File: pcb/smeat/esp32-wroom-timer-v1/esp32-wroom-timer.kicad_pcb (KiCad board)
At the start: 2 copper layers, 49.5 x 51.2 mm, 56 parts, among them J1 Fan_connector, J2 Conn_01x06_Male, J3 input power, Q1 Q_NMOS_GSD, Q2 Q_NMOS_GSD, U1 ESP32-WROOM-32, U2 AMS1117, U3 RX5808, U4 MP1584, U5 RX5808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

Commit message: Update.
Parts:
- added C23: 10µF, Capacitor_SMD:C_0805_2012Metric, B.Cu at (56.8, 60.5)
- added C24: 10µF, Capacitor_SMD:C_0805_2012Metric, B.Cu at (56.8, 63.8)
- R1, R11, R2: value R -> 100k
- R10: value R -> 40.2k
- R12: value R -> 240
- R13: value R -> 390
- R14, R4, R7: value R -> 10k
- R15, R16, R5: value R -> 1k
- R6: value R -> 240k
- R8: value R -> 59k
- R9: value R -> 210k
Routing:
- net GND: track 83.3 -> 89.3 mm, vias 207 -> 208
- net +3V3: track 58.6 -> 61.8 mm

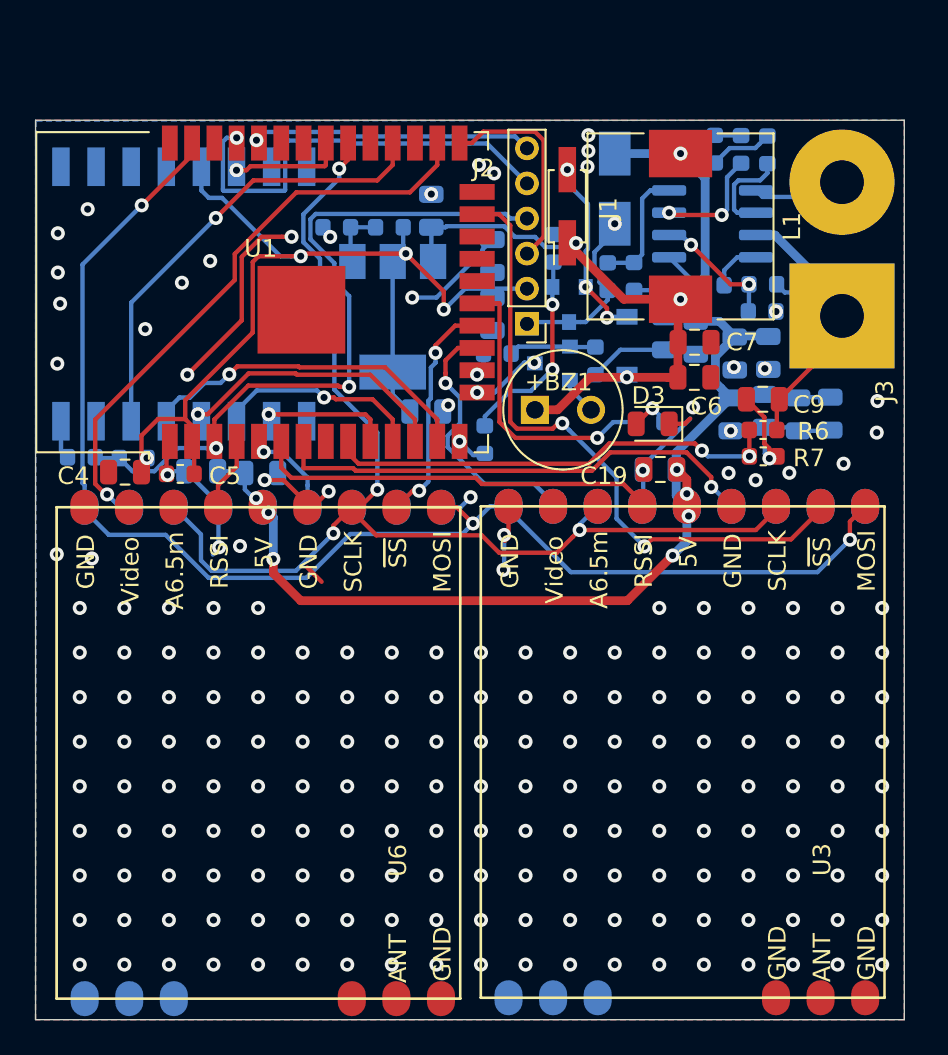
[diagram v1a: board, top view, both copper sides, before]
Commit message: Add a lonely m2 mounting hole Absolutely no space for more than that.
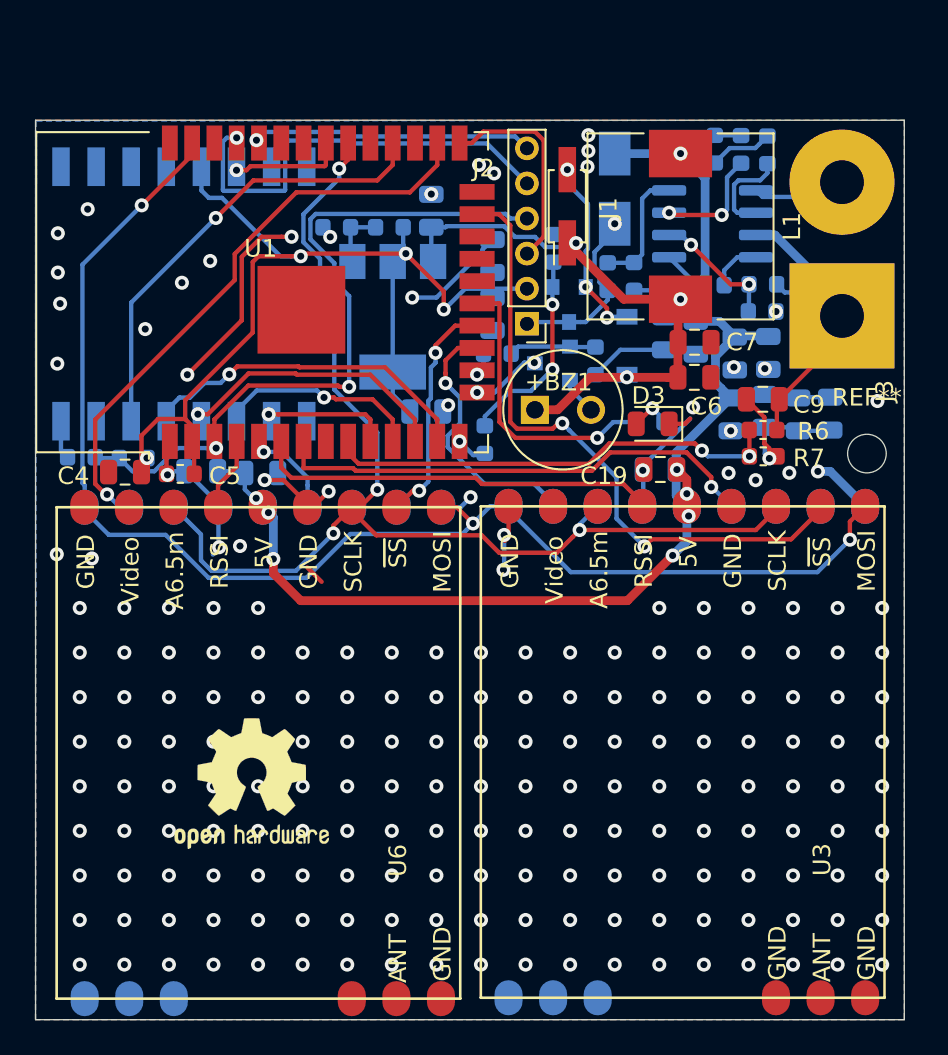
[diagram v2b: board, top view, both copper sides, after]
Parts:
- added REF**: MountingHole_2.2mm_M2, MountingHole:MountingHole_2.2mm_M2, F.Cu at (78.1, 71.8)
- added REF**: OSHW-Logo2_9.8x8mm_SilkScreen, Symbol:OSHW-Logo2_9.8x8mm_SilkScreen, F.Cu at (43.1, 90.6)
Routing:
- net GND: track 89.3 -> 92.8 mm, vias 208 -> 207

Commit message: Disconnect antenna ground from the global ground plane.
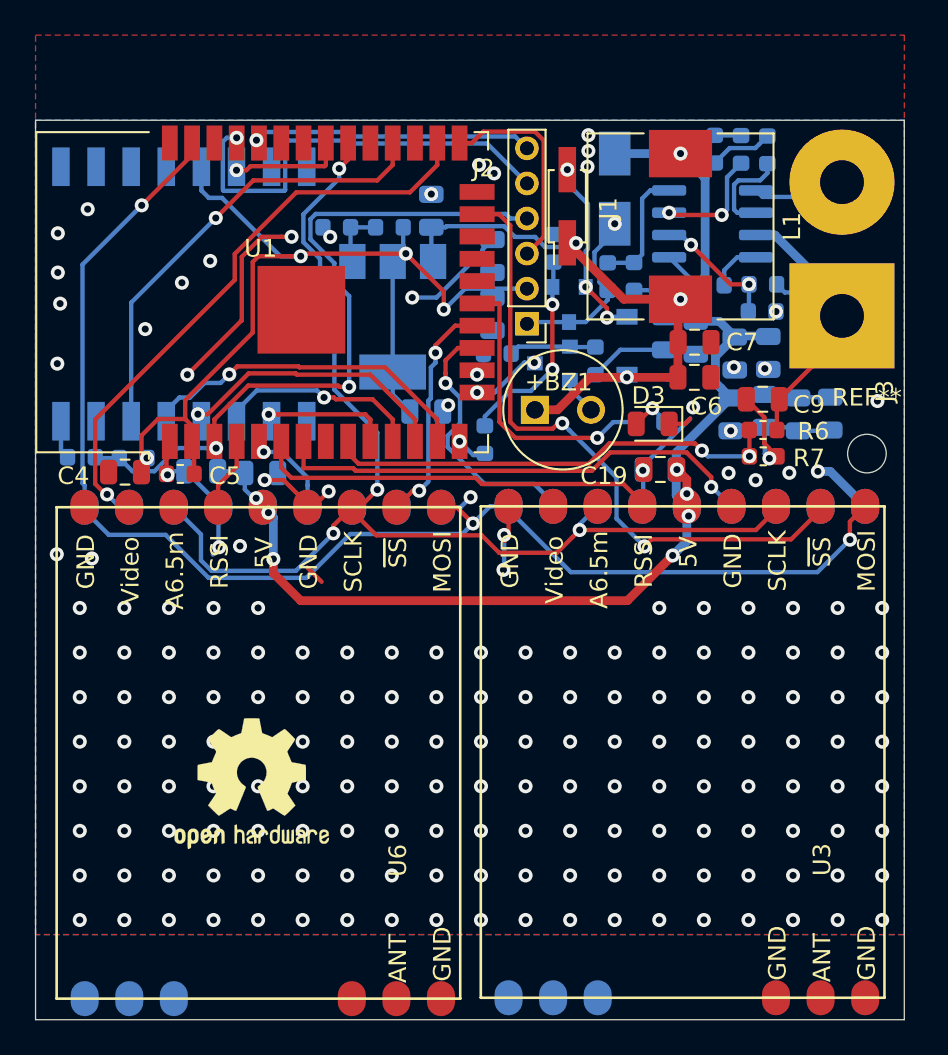
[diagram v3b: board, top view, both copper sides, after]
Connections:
- U3 pad 10: GND -> Net-(U3-Pad10)
- U3 pad 12: GND -> Net-(U3-Pad12)
- U5 pad 10: GND -> Net-(U5-Pad10)
- U5 pad 12: GND -> Net-(U5-Pad12)
- U6 pad 10: GND -> Net-(U6-Pad10)
- U6 pad 12: GND -> Net-(U6-Pad12)
- U7 pad 10: GND -> Net-(U7-Pad10)
- U7 pad 12: GND -> Net-(U7-Pad12)
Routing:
- net GND: vias 207 -> 188
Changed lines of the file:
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@@
     (thickness 1.6)
     (drawings 6)
-    (tracks 778)
+    (tracks 759)
     (zones 0)
     (modules 60)
-    (nets 70)
+    (nets 78)
   )
   (page A4)
@@
   )
   (setup
-    (last_trace_width 0.5)
+    (last_trace_width 0.25)
     (user_trace_width 0.5)
     (trace_clearance 0.15)
@@
   (net 68 "Net-(U1-Pad27)")
   (net 69 "Net-(U1-Pad24)")
+  (net 70 "Net-(U3-Pad12)")
+  (net 71 "Net-(U3-Pad10)")
+  (net 72 "Net-(U5-Pad12)")
+  (net 73 "Net-(U5-Pad10)")
+  (net 74 "Net-(U6-Pad12)")
+  (net 75 "Net-(U6-Pad10)")
+  (net 76 "Net-(U7-Pad12)")
+  (net 77 "Net-(U7-Pad10)")
   (net_class Default "This is the default net class."
     (clearance 0.15)
@@
     (add_net "Net-(U1-Pad36)")
     (add_net "Net-(U1-Pad8)")
+    (add_net "Net-(U3-Pad10)")
     (add_net "Net-(U3-Pad11)")
+    (add_net "Net-(U3-Pad12)")
     (add_net "Net-(U3-Pad2)")
     (add_net "Net-(U3-Pad3)")
+    (add_net "Net-(U5-Pad10)")
     (add_net "Net-(U5-Pad11)")
+    (add_net "Net-(U5-Pad12)")
     (add_net "Net-(U5-Pad2)")
     (add_net "Net-(U5-Pad3)")
+    (add_net "Net-(U6-Pad10)")
     (add_net "Net-(U6-Pad11)")
+    (add_net "Net-(U6-Pad12)")
     (add_net "Net-(U6-Pad2)")
     (add_net "Net-(U6-Pad3)")
+    (add_net "Net-(U7-Pad10)")
     (add_net "Net-(U7-Pad11)")
+    (add_net "Net-(U7-Pad12)")
     (add_net "Net-(U7-Pad2)")
     (add_net "Net-(U7-Pad3)")
@@
       (net 17 /CS4))
     (pad 12 smd oval (at 0 1.1 90) (size 2 1.6) (layers B.Cu B.Paste B.Mask)
-      (net 3 GND))
+      (net 76 "Net-(U7-Pad12)"))
     (pad 11 smd oval (at 0 3.64 90) (size 2 1.6) (layers B.Cu B.Paste B.Mask)
       (net 29 "Net-(U7-Pad11)"))
     (pad 10 smd oval (at 0 6.18 90) (size 2 1.6) (layers B.Cu B.Paste B.Mask)
-      (net 3 GND))
+      (net 77 "Net-(U7-Pad10)"))
     (pad 9 smd oval (at 28 1.1 90) (size 2 1.6) (layers B.Cu B.Paste B.Mask)
       (net 25 /MOSI))
@@
       (net 18 /CS3))
     (pad 12 smd oval (at 0 -1.1 90) (size 2 1.6) (layers F.Cu F.Paste F.Mask)
-      (net 3 GND))
+      (net 74 "Net-(U6-Pad12)"))
     (pad 11 smd oval (at 0 -3.64 90) (size 2 1.6) (layers F.Cu F.Paste F.Mask)
       (net 28 "Net-(U6-Pad11)"))
     (pad 10 smd oval (at 0 -6.18 90) (size 2 1.6) (layers F.Cu F.Paste F.Mask)
-      (net 3 GND))
+      (net 75 "Net-(U6-Pad10)"))
     (pad 9 smd oval (at 28 -1.1 90) (size 2 1.6) (layers F.Cu F.Paste F.Mask)
       (net 25 /MOSI))
@@
       (net 20 /CS2))
     (pad 12 smd oval (at 0 1.1 90) (size 2 1.6) (layers B.Cu B.Paste B.Mask)
-      (net 3 GND))
+      (net 72 "Net-(U5-Pad12)"))
     (pad 11 smd oval (at 0 3.64 90) (size 2 1.6) (layers B.Cu B.Paste B.Mask)
       (net 27 "Net-(U5-Pad11)"))
     (pad 10 smd oval (at 0 6.18 90) (size 2 1.6) (layers B.Cu B.Paste B.Mask)
-      (net 3 GND))
+      (net 73 "Net-(U5-Pad10)"))
     (pad 9 smd oval (at 28 1.1 90) (size 2 1.6) (layers B.Cu B.Paste B.Mask)
       (net 25 /MOSI))
@@
       (net 19 /CS1))
     (pad 12 smd oval (at 0 -1.1 90) (size 2 1.6) (layers F.Cu F.Paste F.Mask)
-      (net 3 GND))
+      (net 70 "Net-(U3-Pad12)"))
     (pad 11 smd oval (at 0 -3.64 90) (size 2 1.6) (layers F.Cu F.Paste F.Mask)
       (net 26 "Net-(U3-Pad11)"))
     (pad 10 smd oval (at 0 -6.18 90) (size 2 1.6) (layers F.Cu F.Paste F.Mask)
-      (net 3 GND))
+      (net 71 "Net-(U3-Pad10)"))
     (pad 9 smd oval (at 28 -1.1 90) (size 2 1.6) (layers F.Cu F.Paste F.Mask)
       (net 25 /MOSI))
@@
     (arrow2b (pts (xy 85.5 104.05) (xy 84.913579 102.923496)))
   )
-  (via (at 75.326 72.81) (size 0.8) (drill 0.4) (layers F.Cu B.Cu) (net 3))
   (via (at 43.322 74.334) (size 0.8) (drill 0.4) (layers F.Cu B.Cu) (net 1))
   (via (at 67.96 75.35) (size 0.8) (drill 0.4) (layers F.Cu B.Cu) (net 1))
@@
   (segment (start 61.2 68.1) (end 62.4 69.3) (width 0.25) (layer B.Cu) (net 2))
   (segment (start 61.2 67.6) (end 61.2 68.1) (width 0.25) (layer B.Cu) (net 2))
+  (via (at 75.326 72.81) (size 0.8) (drill 0.4) (layers F.Cu B.Cu) (net 3))
   (via (at 53.3 57.01) (size 0.8) (drill 0.4) (layers F.Cu B.Cu) (net 3))
   (via (at 59.17 66.61) (size 0.8) (drill 0.4) (layers F.Cu B.Cu) (net 3))
@@
   (via (at 76.45 98.37) (size 0.8) (drill 0.4) (layers F.Cu B.Cu) (net 3))
   (via (at 78.99 98.37) (size 0.8) (drill 0.4) (layers F.Cu B.Cu) (net 3))
-  (via (at 33.27 100.91) (size 0.8) (drill 0.4) (layers F.Cu B.Cu) (net 3))
-  (via (at 35.81 100.91) (size 0.8) (drill 0.4) (layers F.Cu B.Cu) (net 3))
-  (via (at 38.35 100.91) (size 0.8) (drill 0.4) (layers F.Cu B.Cu) (net 3))
-  (via (at 40.89 100.91) (size 0.8) (drill 0.4) (layers F.Cu B.Cu) (net 3))
-  (via (at 43.43 100.91) (size 0.8) (drill 0.4) (layers F.Cu B.Cu) (net 3))
-  (via (at 45.97 100.91) (size 0.8) (drill 0.4) (layers F.Cu B.Cu) (net 3))
-  (via (at 48.51 100.91) (size 0.8) (drill 0.4) (layers F.Cu B.Cu) (net 3))
-  (via (at 51.05 100.91) (size 0.8) (drill 0.4) (layers F.Cu B.Cu) (net 3))
-  (via (at 53.59 100.91) (size 0.8) (drill 0.4) (layers F.Cu B.Cu) (net 3))
-  (via (at 56.13 100.91) (size 0.8) (drill 0.4) (layers F.Cu B.Cu) (net 3))
-  (via (at 58.67 100.91) (size 0.8) (drill 0.4) (layers F.Cu B.Cu) (net 3))
-  (via (at 61.21 100.91) (size 0.8) (drill 0.4) (layers F.Cu B.Cu) (net 3))
-  (via (at 63.75 100.91) (size 0.8) (drill 0.4) (layers F.Cu B.Cu) (net 3))
-  (via (at 66.29 100.91) (size 0.8) (drill 0.4) (layers F.Cu B.Cu) (net 3))
-  (via (at 68.83 100.91) (size 0.8) (drill 0.4) (layers F.Cu B.Cu) (net 3))
-  (via (at 71.37 100.91) (size 0.8) (drill 0.4) (layers F.Cu B.Cu) (net 3))
-  (via (at 73.91 100.91) (size 0.8) (drill 0.4) (layers F.Cu B.Cu) (net 3))
-  (via (at 76.45 100.91) (size 0.8) (drill 0.4) (layers F.Cu B.Cu) (net 3))
-  (via (at 78.99 100.91) (size 0.8) (drill 0.4) (layers F.Cu B.Cu) (net 3))
   (via (at 33.27 80.59) (size 0.8) (drill 0.4) (layers F.Cu B.Cu) (net 3))
   (segment (start 57.45 76.43) (end 57.45 78.38) (width 0.25) (layer B.Cu) (net 3))
@@
     (polygon
       (pts
-        (xy 30.8 52.85) (xy 80.25 52.8) (xy 80.25 104.05) (xy 30.75 104.05)
+        (xy 30.75 52.8) (xy 80.25 52.8) (xy 80.25 99.2) (xy 30.75 99.2)
       )
     )
@@
     (polygon
       (pts
-        (xy 30.75 52.8) (xy 80.25 52.8) (xy 80.25 104.05) (xy 30.75 104.05)
+        (xy 30.75 47.95) (xy 80.25 47.95) (xy 80.25 99.2) (xy 30.75 99.2)
       )
     )
